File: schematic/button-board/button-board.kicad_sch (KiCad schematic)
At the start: 47 parts, among them J10 Conn_01x04_Socket, J11 Conn_01x04_Socket, J12 Conn_01x04_Socket, J13 Conn_01x04_Socket, J14 Conn_01x04_Socket, J16 Screw_Terminal_01x06, J2 Screw_Terminal_01x08, J3 Screw_Terminal_01x08, J7 Conn_01x04_Socket, J8 Conn_01x04_Socket, J9 Conn_01x04_Socket, Q10 2N7002, Q11 2N7002, Q12 2N7002, Q4 2N7002, Q5 2N7002, Q6 2N7002, Q7 2N7002, Q9 2N7002, U1 MCP23017_SO

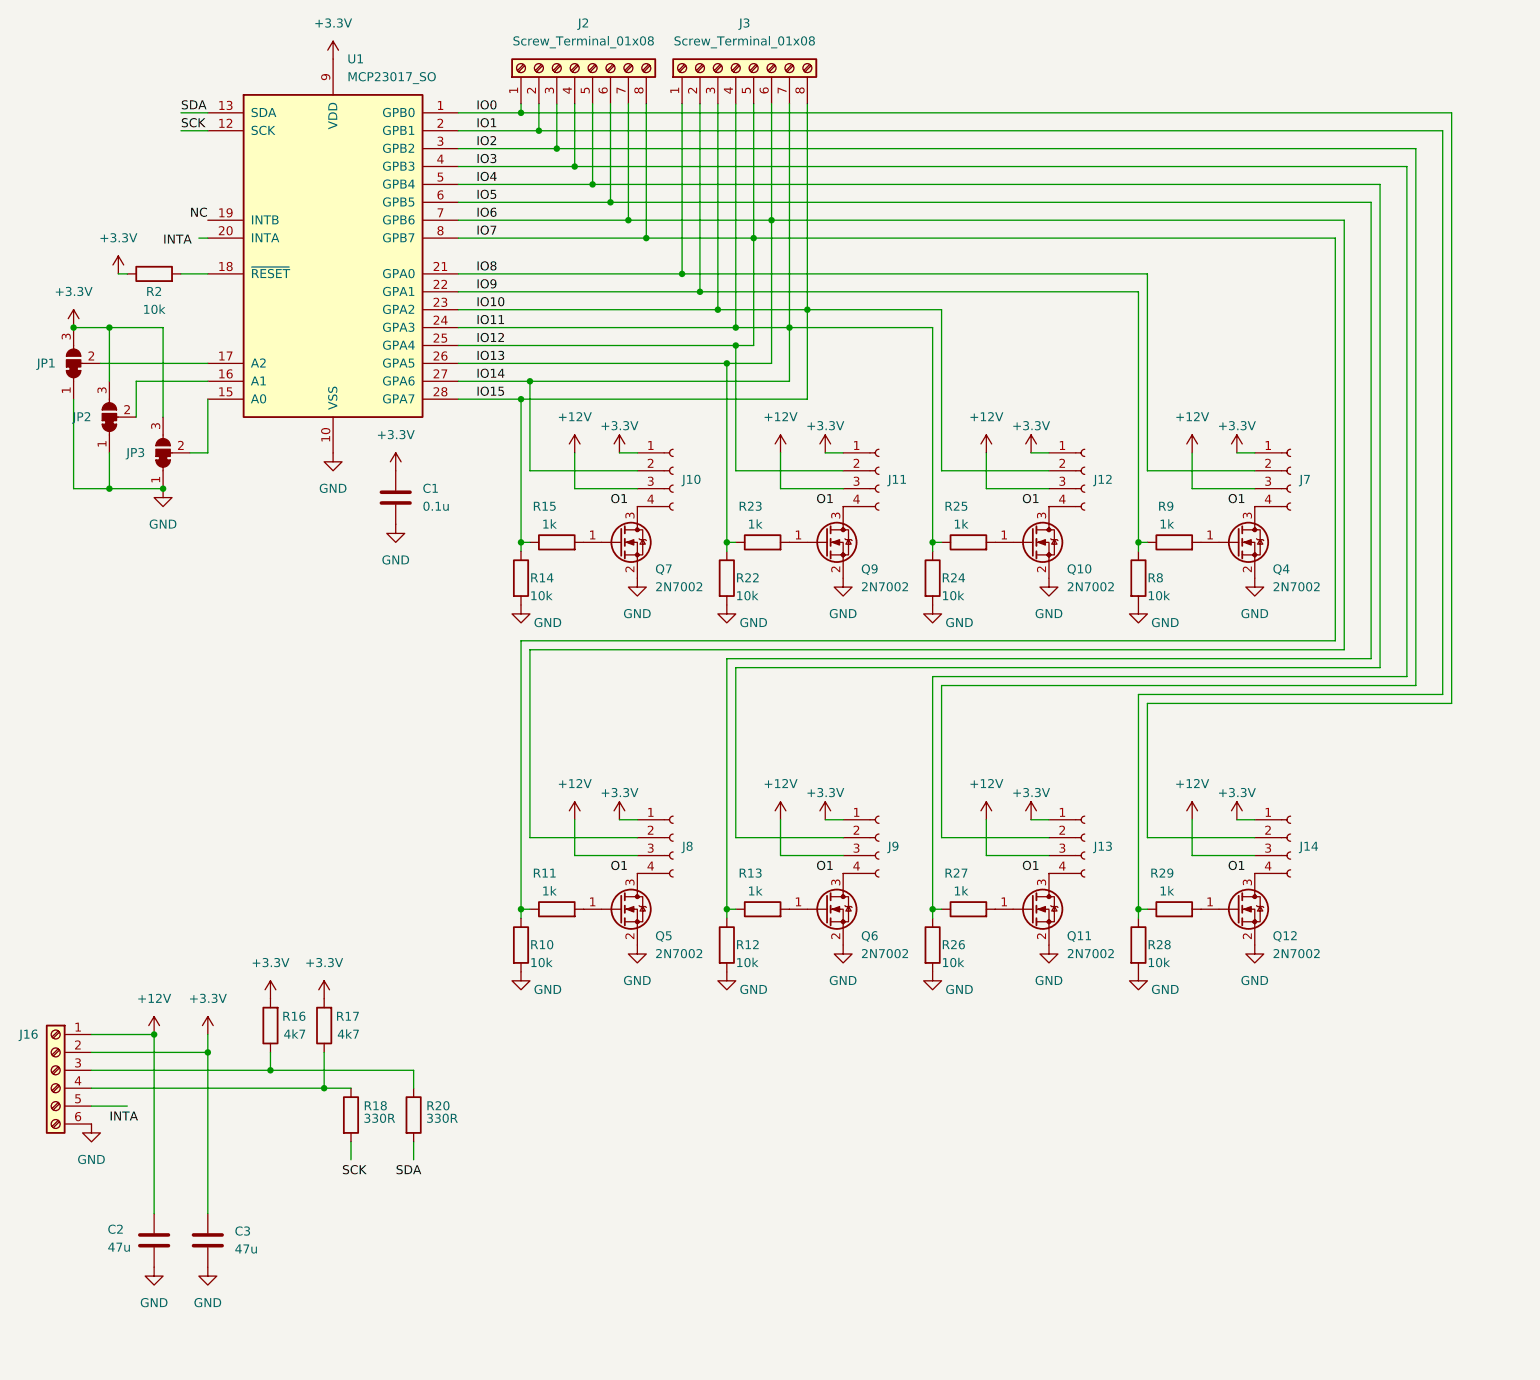
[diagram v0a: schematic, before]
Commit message: renamed board
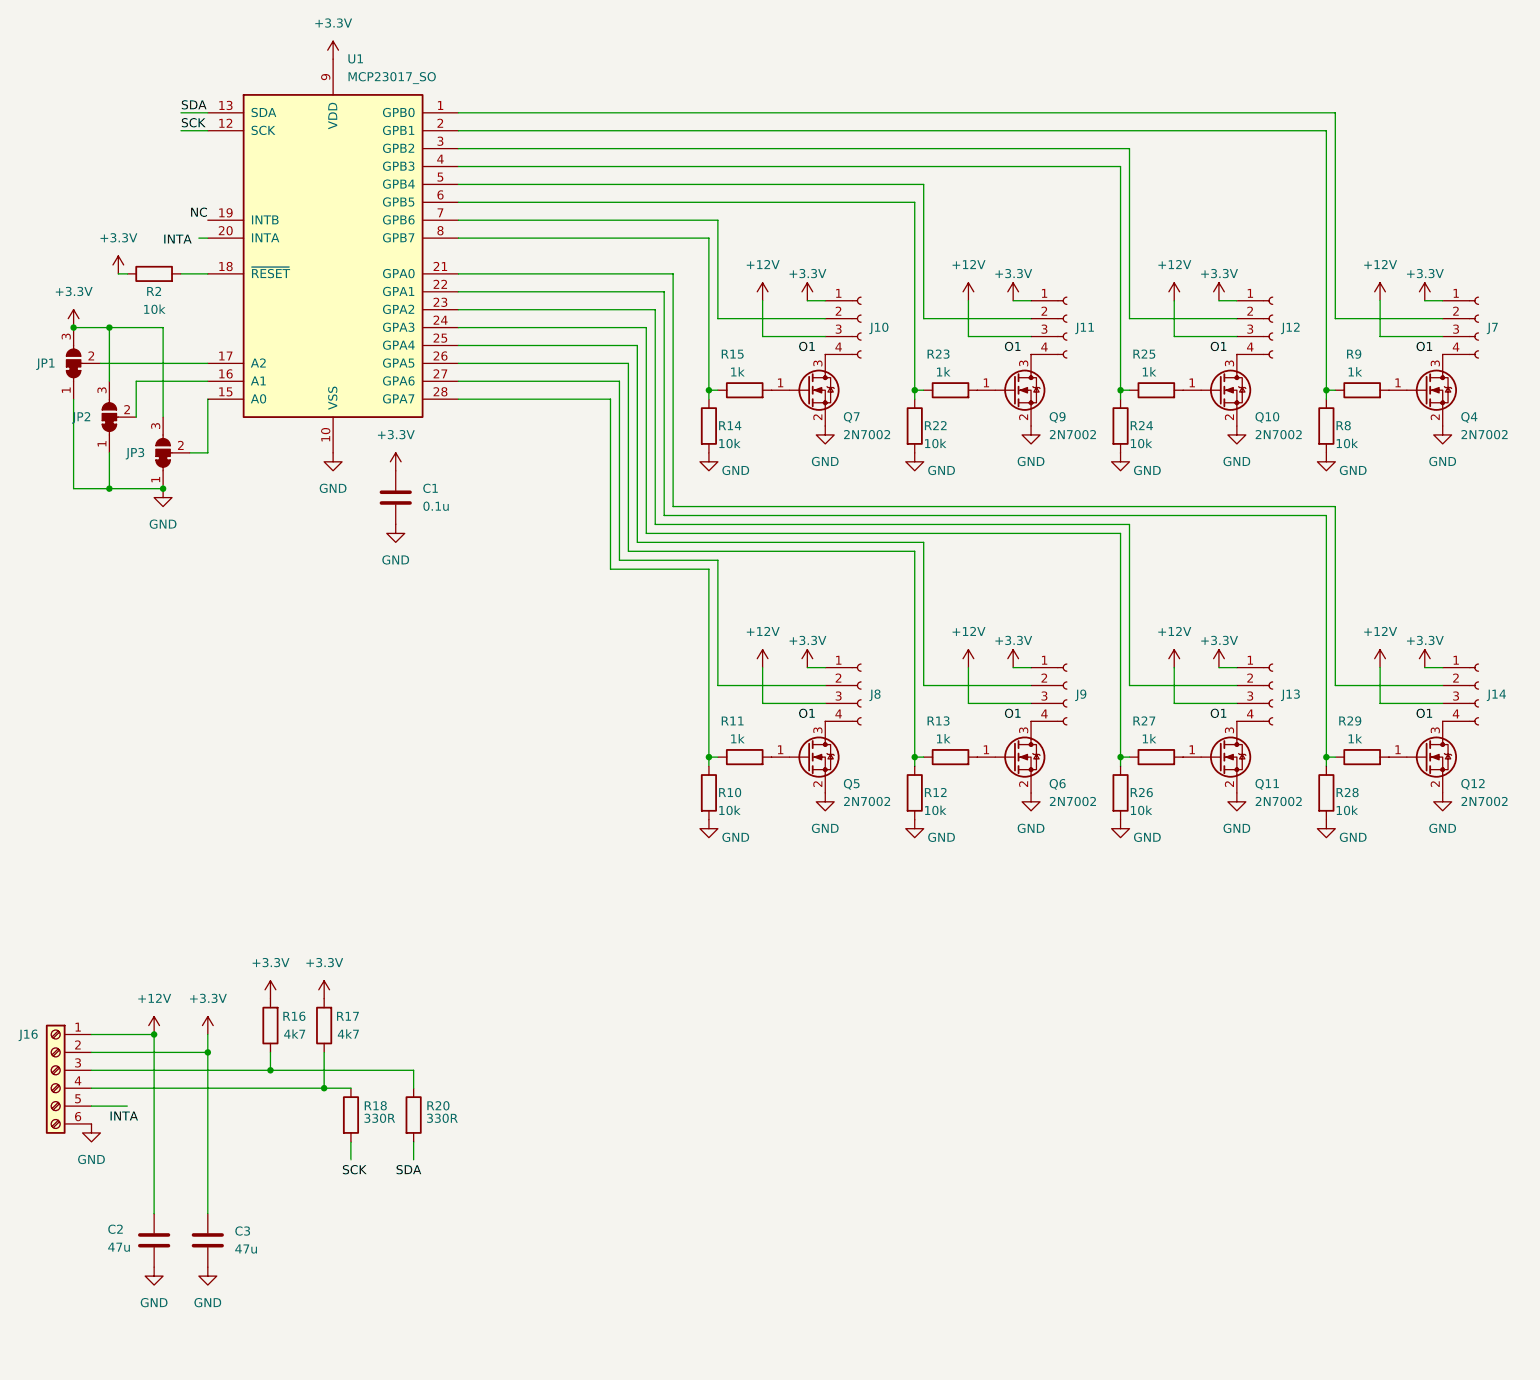
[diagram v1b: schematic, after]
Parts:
- removed J2, J3: Screw_Terminal_01x08, TerminalBlock:TerminalBlock_bornier-8_P5.08mm, symbol Connector:Screw_Terminal_01x08
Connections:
- net IO0: no longer names the net of U1.1 (GPB0)
- net IO0: now also J7.2 (Pin_2); no longer J14.2 (Pin_2)
- net IO1: no longer names the net of R28.1, R29.1
- net IO1: now also U1.22 (GPA1); no longer U1.2 (GPB1)
- removed net IO10: J12.2 (Pin_2), R14.1, R15.1, U1.23 (GPA2), U1.28 (GPA7)
- removed net IO11: J10.2 (Pin_2), R24.1, R25.1, U1.24 (GPA3), U1.27 (GPA6)
- removed net IO12: J11.2 (Pin_2), R10.1, R11.1, U1.25 (GPA4), U1.8 (GPB7)
- removed net IO13: J8.2 (Pin_2), R22.1, R23.1, U1.26 (GPA5), U1.7 (GPB6)
- net IO2: no longer names the net of U1.3 (GPB2)
- net IO2: now also J12.2 (Pin_2); no longer J13.2 (Pin_2)
- net IO3: no longer names the net of R26.1, R27.1
- net IO3: now also U1.24 (GPA3); no longer U1.4 (GPB3)
- net IO4: no longer names the net of U1.5 (GPB4)
- net IO4: now also J11.2 (Pin_2); no longer J9.2 (Pin_2)
- net IO5: no longer names the net of R12.1, R13.1
- net IO5: now also U1.26 (GPA5); no longer U1.6 (GPB5)
- net IO8: no longer names the net of U1.21 (GPA0)
- net IO8: now also J14.2 (Pin_2); no longer J7.2 (Pin_2)
- net IO9: no longer names the net of R8.1, R9.1
- net IO9: now also U1.2 (GPB1); no longer U1.22 (GPA1)
- new net: R24.1, R25.1, U1.4 (GPB3)
- new net: R10.1, R11.1, U1.28 (GPA7)
- new net: R14.1, R15.1, U1.8 (GPB7)
- new net: J9.2 (Pin_2), U1.25 (GPA4)
- new net: J8.2 (Pin_2), U1.27 (GPA6)
- new net: J13.2 (Pin_2), U1.23 (GPA2)
- new net: R22.1, R23.1, U1.6 (GPB5)
- new net: J10.2 (Pin_2), U1.7 (GPB6)
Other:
- moved on the sheet: J10, J11, J12, J13, J14, J7, J8, J9, Q10, Q11, Q12, Q4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

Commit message: finalized button board, added sensor board
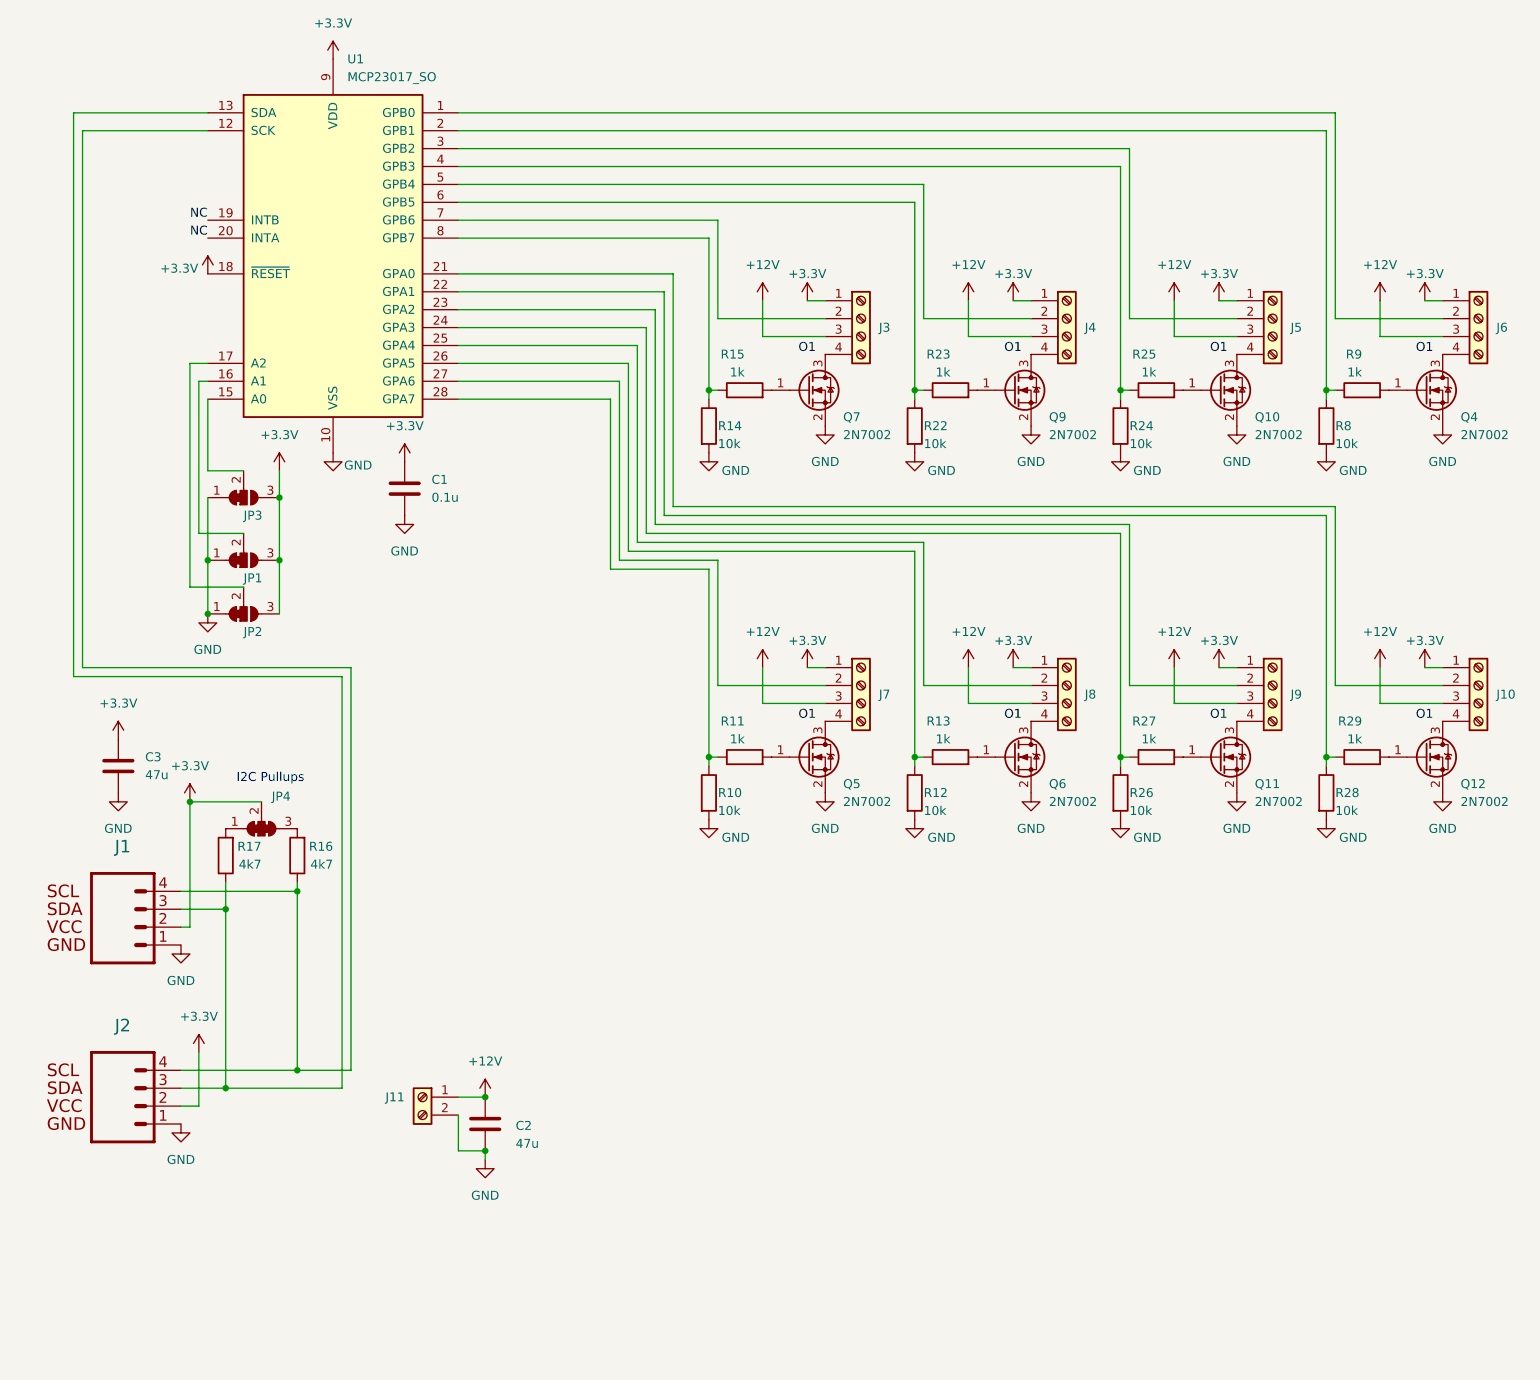
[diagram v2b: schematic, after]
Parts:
- removed J10, J11, J12, J13, J14, J7, J8, J9: Conn_01x04_Socket, Connector_JST:JST_XH_B4B-XH-AM_1x04_P2.50mm_Vertical, symbol Connector:Conn_01x04_Socket
- removed J16: Screw_Terminal_01x06, TerminalBlock:TerminalBlock_bornier-6_P5.08mm, symbol Connector:Screw_Terminal_01x06
- removed R18, R20: 330R, Resistor_SMD:R_0805_2012Metric, symbol Device:R
- removed R2: 10k, Resistor_SMD:R_0805_2012Metric, symbol Device:R
- added J1, J2: ~, SparkFun-Connectors:JST04_1MM_VERT, symbol SparkFun-Connectors:QWIIC_CONNECTOR
- added J10, J3, J4, J5, J6, J7, J8, J9: Screw_Terminal_01x04, TerminalBlock_Phoenix:TerminalBlock_Phoenix_MKDS-1,5-4-5.08_1x04_P5.08mm_Horizontal, symbol Connector:Screw_Terminal_01x04
- added J11: Screw_Terminal_01x02, TerminalBlock_Phoenix:TerminalBlock_Phoenix_MKDS-1,5-2-5.08_1x02_P5.08mm_Horizontal, symbol Connector:Screw_Terminal_01x02
- added JP4: SolderJumper_3_Bridged123, Jumper:SolderJumper-3_P1.3mm_Bridged123_RoundedPad1.0x1.5mm_NumberLabels, symbol Jumper:SolderJumper_3_Bridged123
- JP1, JP2, JP3: footprint Jumper:SolderJumper-3_P1.3mm_Bridged12_RoundedPad1.0x1.5mm -> Jumper:SolderJumper-3_P1.3mm_Bridged12_RoundedPad1.0x1.5mm_NumberLabels
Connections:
- net SCK is gone; now on an unnamed net: U1.12 (SCK)
- net SDA is gone; now on an unnamed net: U1.13 (SDA)
- net +12V: now also J10.3 (Pin_3), J11.1 (Pin_1), J3.3 (Pin_3), J4.3 (Pin_3), J5.3 (Pin_3), J6.3 (Pin_3), J7.3 (Pin_3), J8.3 (Pin_3), J9.3 (Pin_3)
- net +3.3V: now also U1.18 (~{RESET}), J1.2, J10.1 (Pin_1), J2.2, J3.1 (Pin_1), J4.1 (Pin_1), J5.1 (Pin_1), J6.1 (Pin_1), J7.1 (Pin_1), J8.1 (Pin_1), J9.1 (Pin_1), JP4.2 (C); no longer R16.2, R17.2
- net GND: now also J1.1, J11.2 (Pin_2), J2.1
- net at Q10.3 (D): now also J5.4 (Pin_4)
- net at R16.1: now also J1.4, J2.4
- net at R17.1: now also J1.3, J2.3
- net at U1.3 (GPB2): now also J5.2 (Pin_2)
- net at Q4.3 (D): now also J6.4 (Pin_4)
- net at U1.17 (A2): now also JP2.2 (C); no longer JP1.2 (C)
- net at U1.1 (GPB0): now also J6.2 (Pin_2)
- net at Q5.3 (D): now also J7.4 (Pin_4)
- net at U1.5 (GPB4): now also J4.2 (Pin_2)
- net at Q9.3 (D): now also J4.4 (Pin_4)
- net at U1.25 (GPA4): now also J8.2 (Pin_2)
- net at Q6.3 (D): now also J8.4 (Pin_4)
- net at U1.27 (GPA6): now also J7.2 (Pin_2)
- net at Q12.3 (D): now also J10.4 (Pin_4)
- net at U1.16 (A1): now also JP1.2 (C); no longer JP2.2 (C)
- net at U1.21 (GPA0): now also J10.2 (Pin_2)
- net at U1.23 (GPA2): now also J9.2 (Pin_2)
- net at U1.7 (GPB6): now also J3.2 (Pin_2)
- net at Q7.3 (D): now also J3.4 (Pin_4)
- net at Q11.3 (D): now also J9.4 (Pin_4)
- new net: JP4.1 (A), R17.2
- new net: JP4.3 (B), R16.2
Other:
- note added: "I2C Pullups"
- title: (none) -> Makeomatic 750 Button Board
- moved on the sheet: C1, C2, C3, JP3, R16, R17

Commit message: replaced individual transistors with array
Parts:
- removed Q10, Q11, Q12, Q4, Q5, Q6, Q7, Q9: 2N7002, Package_TO_SOT_SMD:SOT-23, symbol Transistor_FET:2N7002
- removed R10, R12, R14, R22, R24, R26, R28: 10k, Resistor_SMD:R_0805_2012Metric, symbol Device:R
- removed R11, R13, R15, R23, R25, R27, R29, R9: 1k, Resistor_SMD:R_0805_2012Metric, symbol Device:R
- added R1, R2, R3, R4, R5, R6, R7: 1k, Resistor_SMD:R_0805_2012Metric, symbol Device:R
- added U2: ULN2803A, symbol Transistor_Array:ULN2803A
- R8: value 10k -> 1k
- renumbered J1 to J11, J2 to J12
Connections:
- net +12V: now also U2.10 (COM)
- net GND: now also U2.9 (GND); no longer R8.2
- net at U1.2 (GPB1): now also R2.2; no longer R8.1
- net at J5.4 (Pin_4): now also U2.15 (O4)
- net at J5.2 (Pin_2): now also R4.1; no longer U1.3 (GPB2)
- net at U1.22 (GPA1): now also U2.2 (I2)
- net at U1.24 (GPA3): now also U2.4 (I4)
- net at J6.4 (Pin_4): now also U2.18 (O1)
- net at U1.26 (GPA5): now also U2.6 (I6)
- net at U1.4 (GPB3): now also R4.2
- net at U1.28 (GPA7): now also U2.8 (I8)
- net at U1.8 (GPB7): now also R8.2
- net at U1.5 (GPB4): now also R5.2; no longer J4.2 (Pin_2)
- net at J4.4 (Pin_4): now also U2.16 (O3)
- net at J7.4 (Pin_4): now also U2.14 (O5)
- net at J3.2 (Pin_2): now also R2.1; no longer U1.7 (GPB6)
- net at J3.4 (Pin_4): now also U2.17 (O2)
- net at U1.25 (GPA4): now also U2.5 (I5); no longer J8.2 (Pin_2)
- net at J8.4 (Pin_4): now also U2.13 (O6)
- net at U1.21 (GPA0): now also U2.1 (I1); no longer J10.2 (Pin_2)
- net at J10.4 (Pin_4): now also U2.11 (O8)
- net at J6.2 (Pin_2): now also R1.1; no longer U1.1 (GPB0)
- net at U1.23 (GPA2): now also U2.3 (I3); no longer J9.2 (Pin_2)
- net at J7.2 (Pin_2): now also R5.1; no longer U1.27 (GPA6)
- net at U1.6 (GPB5): now also R6.2
- net at J9.4 (Pin_4): now also U2.12 (O7)
- new net: R1.2, U1.1 (GPB0)
- new net: U1.27 (GPA6), U2.7 (I7)
- new net: J4.2 (Pin_2), R3.1
- new net: J9.2 (Pin_2), R7.1
- new net: R7.2, U1.7 (GPB6)
- new net: R3.2, U1.3 (GPB2)
- new net: J10.2 (Pin_2), R8.1
- new net: J8.2 (Pin_2), R6.1
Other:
- moved on the sheet: C1, C2, C3, J11, J12, J6, JP1, JP2, JP3, JP4, R16, R17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

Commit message: layout work
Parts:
- J1: renamed from J11; footprint SparkFun-Connectors:JST04_1MM_VERT -> 1x04_RA_SMD
- J2: renamed from J12; footprint SparkFun-Connectors:JST04_1MM_VERT -> 1x04_RA_SMD
- U2: footprint (none) -> Package_SO:SOP-18_7.495x11.515mm_P1.27mm
- renumbered C3 to C1, C1 to C2, C2 to C3, J9 to J10, J10 to J11, J11 to J3, J6 to J4, J3 to J5, J4 to J6, J5 to J7, J7 to J8, J8 to J9, JP3 to JP1, JP1 to JP2, JP2 to JP3, R17 to R1, R8 to R10, R16 to R2, R1 to R3, R2 to R4, R3 to R5, R4 to R6, R5 to R7, R6 to R8, R7 to R9
